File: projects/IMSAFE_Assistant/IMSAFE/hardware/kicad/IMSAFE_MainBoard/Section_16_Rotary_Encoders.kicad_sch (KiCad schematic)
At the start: 8 parts

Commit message: Add sensor and interface schematic implementations
- Section 01: MCU Core additional connections
- Section 04: BMS refinements
- Section 07: Barometric sensor (BMP390)
- Section 08: IMU (ICM-42688-P) full implementation
- Section 09: Magnetometer (MMC5983MA) full implementation
- Section 10: Gas sensor (MICS-4514) with heater control
- Section 11: Temp/Humidity (Si7021-A20) implementation
- Section 14: I/O Expander updates
- Section 16: Rotary encoder connections
- Section 19: Audio buzzer (MLT-8530) with MOSFET driver

Co-Authored-By: Claude Opus 4.5 <noreply@anthropic.com>
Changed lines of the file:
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@@
 		(instances (project "IMSAFE_MainBoard" (path "/sec16-0001-0002-0003-000000000001" (reference "#PWR1606") (unit 1))))
+	)
+	(symbol (lib_id "power:GND") (at 104.14 111.76 0) (unit 1)
+		(exclude_from_sim no) (in_bom yes) (on_board yes) (dnp no)
+		(uuid "pwr-gnd-enc1-s2")
+		(property "Reference" "#PWR1607" (at 104.14 118.11 0) (effects (font (size 1.27 1.27)) hide))
+		(property "Value" "GND" (at 104.14 115.57 0) (effects (font (size 1.27 1.27)) hide))
+		(property "Footprint" "" (at 104.14 111.76 0) (effects (font (size 1.27 1.27)) hide))
+		(property "Datasheet" "" (at 104.14 111.76 0) (effects (font (size 1.27 1.27)) hide))
+		(pin "1" (uuid "pwr-gnd-enc1-s2-p1"))
+		(instances (project "IMSAFE_MainBoard" (path "/sec16-0001-0002-0003-000000000001" (reference "#PWR1607") (unit 1))))
+	)
+	(symbol (lib_id "power:GND") (at 200.66 111.76 0) (unit 1)
+		(exclude_from_sim no) (in_bom yes) (on_board yes) (dnp no)
+		(uuid "pwr-gnd-enc2-s2")
+		(property "Reference" "#PWR1608" (at 200.66 118.11 0) (effects (font (size 1.27 1.27)) hide))
+		(property "Value" "GND" (at 200.66 115.57 0) (effects (font (size 1.27 1.27)) hide))
+		(property "Footprint" "" (at 200.66 111.76 0) (effects (font (size 1.27 1.27)) hide))
+		(property "Datasheet" "" (at 200.66 111.76 0) (effects (font (size 1.27 1.27)) hide))
+		(pin "1" (uuid "pwr-gnd-enc2-s2-p1"))
+		(instances (project "IMSAFE_MainBoard" (path "/sec16-0001-0002-0003-000000000001" (reference "#PWR1608") (unit 1))))
 	)
 	(wire (pts (xy 93.98 123.19) (xy 93.98 132.08)) (stroke (width 0) (type default)) (uuid "w-enc1-com-gnd"))

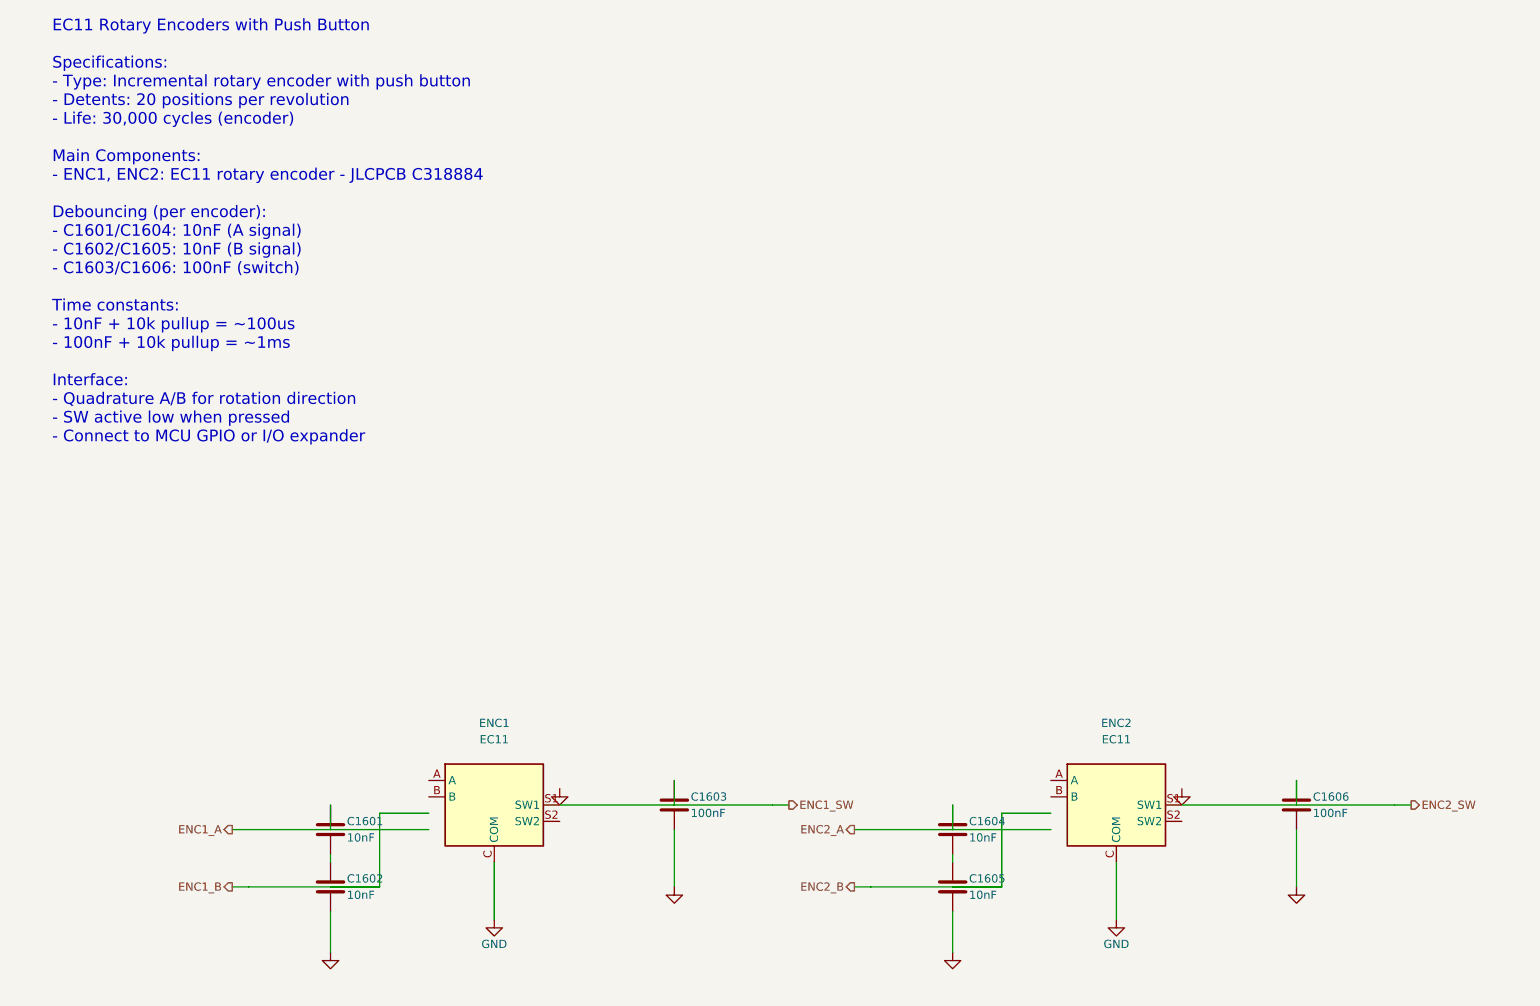
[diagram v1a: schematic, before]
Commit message: Update KiCad schematics and add analysis files
- Update all MainBoard schematic sections with component placement
- Add ERC reports and analysis scripts for schematic validation
- Update Radar Interface and SwitchLED Board projects
- Sync KiCad project files with latest session changes

Co-Authored-By: Claude Opus 4.5 <noreply@anthropic.com>
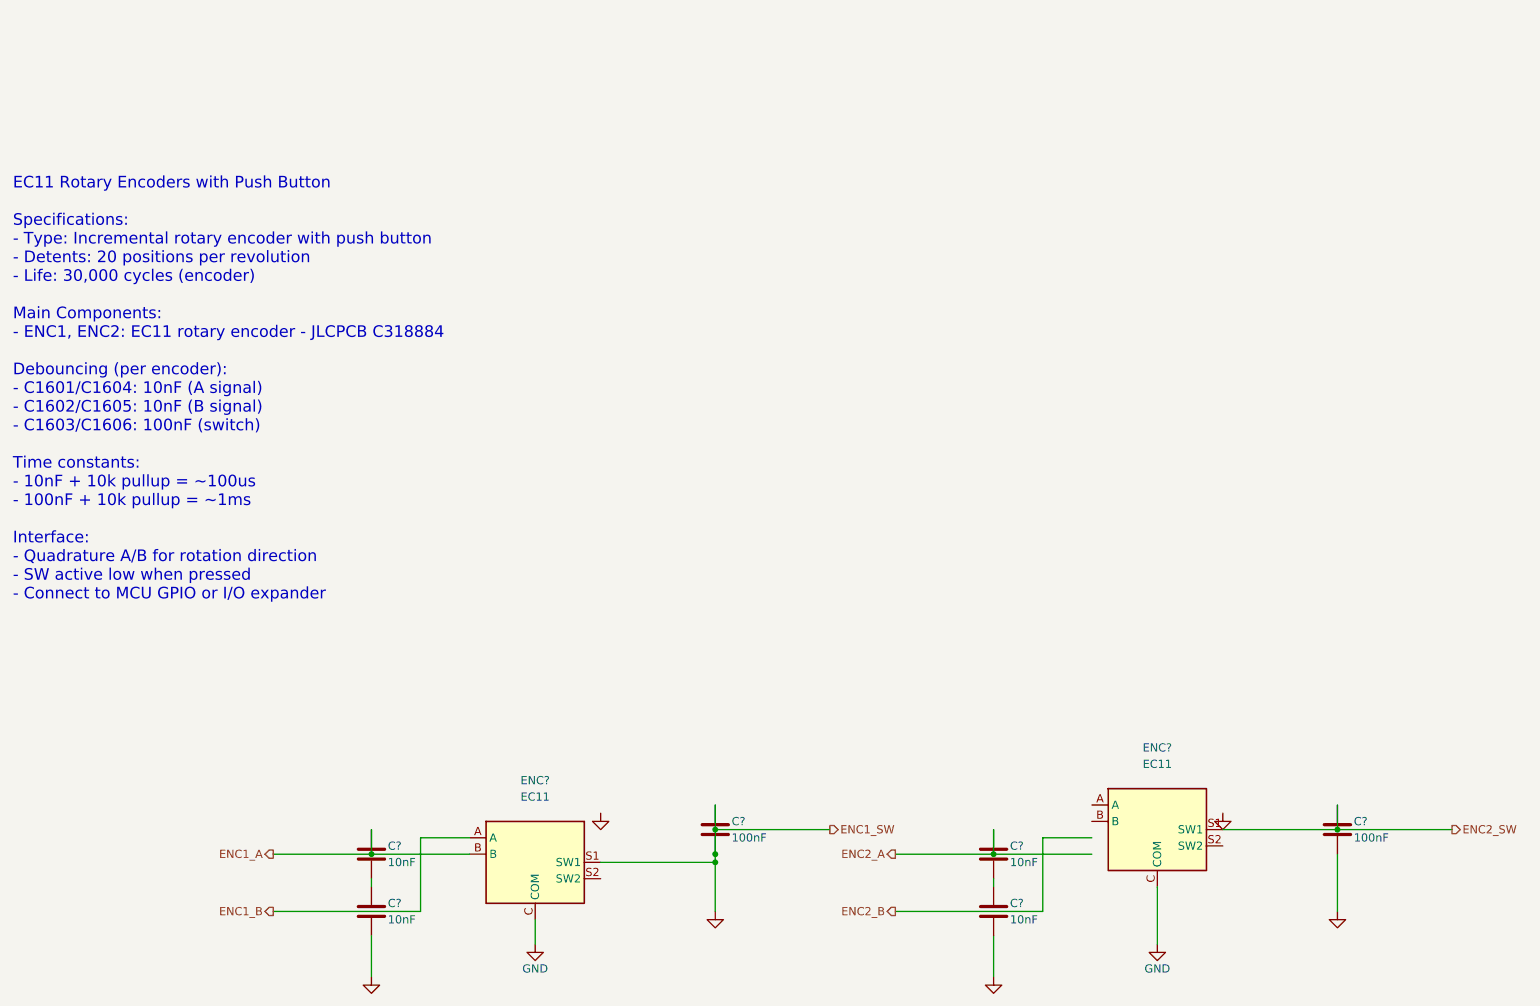
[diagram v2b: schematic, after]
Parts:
- removed C1601, C1602, C1604, C1605: 10nF, Capacitor_SMD:C_0603_1608Metric, symbol Device:C
- removed C1603, C1606: 100nF, Capacitor_SMD:C_0603_1608Metric, symbol Device:C
- removed ENC1, ENC2: EC11, Rotary_Encoder:RotaryEncoder_Alps_EC11E-Switch_Vertical_H20mm, symbol Switch:EC11
- added C? (x4): 10nF, Capacitor_SMD:C_0603_1608Metric, symbol Device:C
- added C? (x2): 100nF, Capacitor_SMD:C_0603_1608Metric, symbol Device:C
- added ENC? (x2): EC11, Rotary_Encoder:RotaryEncoder_Alps_EC11E-Switch_Vertical_H20mm, symbol Switch:EC11
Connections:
- net ENC1_A: now also C?.1, ENC?.B
- net ENC1_B: now also ENC?.A
- net ENC2_A: now also C?.1
- net ENC2_SW: now also C?.1, ENC?.S1 (SW1)
- net GND: now also C?.1, C?.2, C?.2, C?.2, C?.2, ENC?.C (COM), ENC?.C (COM), ENC?.S1 (SW1)
- new net: C?.1, C?.2 (x2)
